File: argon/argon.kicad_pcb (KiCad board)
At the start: 2 copper layers, 60 x 60 mm, 77 parts, among them J1 USB, J2 V3V3-GND, J3 V3V3-GND, J4 V3V3-GND, J5 V3V3-GND, J6 V3V3-GND, J7 V3V3-GND, U1 LMC555xM, U2 AMS1117-3.3, U3 93LCxxA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

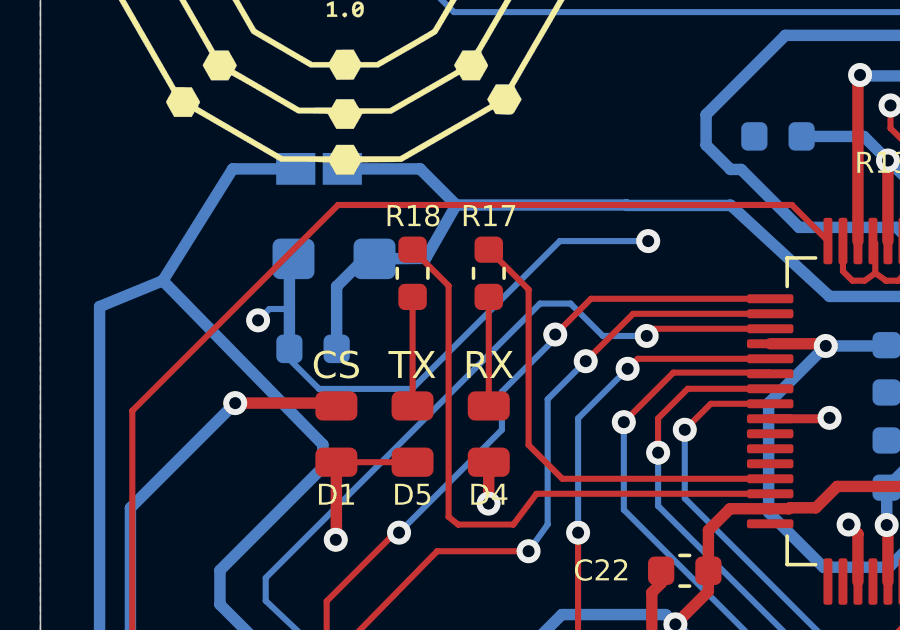
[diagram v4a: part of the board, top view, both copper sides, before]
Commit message: Small paths adjustments
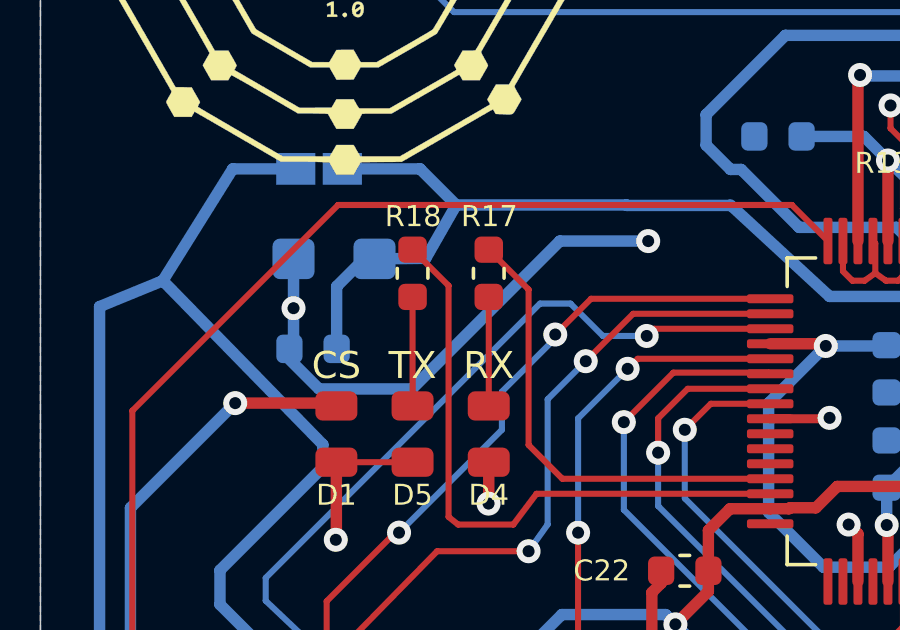
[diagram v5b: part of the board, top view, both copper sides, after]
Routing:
- net GND: track 122.4 -> 121.4 mm
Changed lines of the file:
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@@
     (thickness 1.6)
     (drawings 54)
-    (tracks 713)
+    (tracks 712)
     (zones 0)
     (modules 77)
@@
   (layers
     (0 F.Cu signal)
-    (31 B.Cu signal hide)
+    (31 B.Cu signal)
     (32 B.Adhes user hide)
     (33 F.Adhes user hide)
     (34 B.Paste user hide)
     (35 F.Paste user hide)
-    (36 B.SilkS user hide)
+    (36 B.SilkS user)
     (37 F.SilkS user)
     (38 B.Mask user hide)
@@
   )
   (setup
-    (last_trace_width 0.2032)
+    (last_trace_width 0.381)
     (user_trace_width 0.2032)
     (user_trace_width 0.3)
@@
   (segment (start 140.6905 114.7319) (end 140.38 115.0424) (width 0.381) (layer F.Cu) (net 1))
   (segment (start 140.6745 114.3) (end 140.6905 114.316) (width 0.381) (layer F.Cu) (net 1))
-  (segment (start 128.2985 104.0575) (end 128.436 103.92) (width 0.381) (layer B.Cu) (net 1))
   (segment (start 128.2985 106.92) (end 128.2985 107.2673) (width 0.2032) (layer B.Cu) (net 1))
-  (segment (start 128.2985 107.2673) (end 129.286 108.2548) (width 0.2032) (layer B.Cu) (net 1))
-  (segment (start 129.286 108.2548) (end 132.3848 108.2548) (width 0.2032) (layer B.Cu) (net 1))
-  (via (at 140.2588 103.3272) (size 0.8) (drill 0.4) (layers F.Cu B.Cu) (net 1))
-  (segment (start 132.3848 108.2548) (end 137.3124 103.3272) (width 0.2032) (layer B.Cu) (net 1))
-  (segment (start 137.3124 103.3272) (end 140.2588 103.3272) (width 0.2032) (layer B.Cu) (net 1))
-  (segment (start 128.2985 105.5909) (end 128.2985 104.0575) (width 0.381) (layer B.Cu) (net 1))
-  (segment (start 128.2985 106.92) (end 128.2985 105.5909) (width 0.381) (layer B.Cu) (net 1))
   (segment (start 160.655 97.393) (end 160.655 96.901) (width 0.2032) (layer F.Cu) (net 1))
   (segment (start 162.5 123.927) (end 162.5 125.028) (width 0.381) (layer B.Cu) (net 1))
@@
   (segment (start 149.7965 99.5045) (end 149.098 98.806) (width 0.2032) (layer B.Cu) (net 1))
   (segment (start 149.098 98.806) (end 148.336 98.806) (width 0.2032) (layer B.Cu) (net 1))
-  (segment (start 128.2985 105.5909) (end 127.6319 105.5909) (width 0.2032) (layer B.Cu) (net 1))
-  (segment (start 127.6319 105.5909) (end 127.254 105.9688) (width 0.2032) (layer B.Cu) (net 1))
-  (via (at 127.254 105.9688) (size 0.8) (drill 0.4) (layers F.Cu B.Cu) (net 1))
   (via (at 129.8448 113.284) (size 0.8) (drill 0.4) (layers F.Cu B.Cu) (net 1))
   (via (at 135.636 125.8316) (size 0.8) (drill 0.4) (layers F.Cu B.Cu) (net 1))
@@
   (segment (start 148.75 102.25) (end 148.75 102.216) (width 0.2032) (layer F.Cu) (net 1))
   (segment (start 148.75 103.325) (end 148.75 102.25) (width 0.2032) (layer F.Cu) (net 1))
+  (segment (start 128.2985 107.2673) (end 129.286 108.2548) (width 0.381) (layer B.Cu) (net 1))
+  (segment (start 129.286 108.2548) (end 132.3848 108.2548) (width 0.381) (layer B.Cu) (net 1))
+  (segment (start 132.3848 108.2548) (end 137.3124 103.3272) (width 0.381) (layer B.Cu) (net 1))
+  (segment (start 137.3124 103.3272) (end 140.2588 103.3272) (width 0.381) (layer B.Cu) (net 1))
+  (via (at 140.2588 103.3272) (size 0.8) (drill 0.4) (layers F.Cu B.Cu) (net 1))
+  (segment (start 128.2985 104.0575) (end 128.436 103.92) (width 0.381) (layer B.Cu) (net 1))
+  (segment (start 128.436 106.7825) (end 128.2985 106.92) (width 0.381) (layer B.Cu) (net 1))
+  (segment (start 128.436 103.92) (end 128.436 105.564) (width 0.381) (layer B.Cu) (net 1))
+  (segment (start 128.436 105.564) (end 128.436 106.7825) (width 0.381) (layer B.Cu) (net 1))
+  (via (at 128.436 105.564) (size 0.8) (drill 0.4) (layers F.Cu B.Cu) (net 1))
   (segment (start 136.503 121.9135) (end 137.687 120.7295) (width 0.381) (layer B.Cu) (net 2))
   (segment (start 134.9595 121.9135) (end 136.503 121.9135) (width 0.381) (layer B.Cu) (net 2))

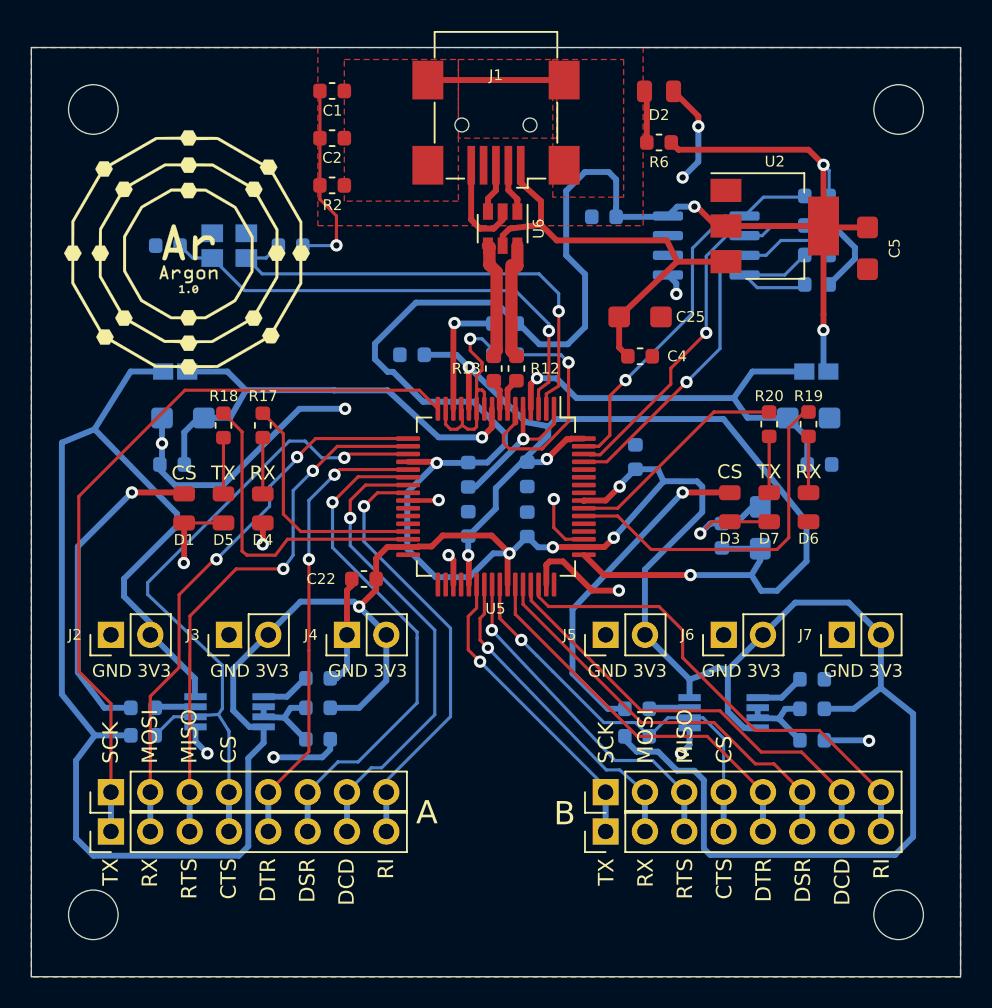
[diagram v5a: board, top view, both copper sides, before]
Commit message: Rounded corners
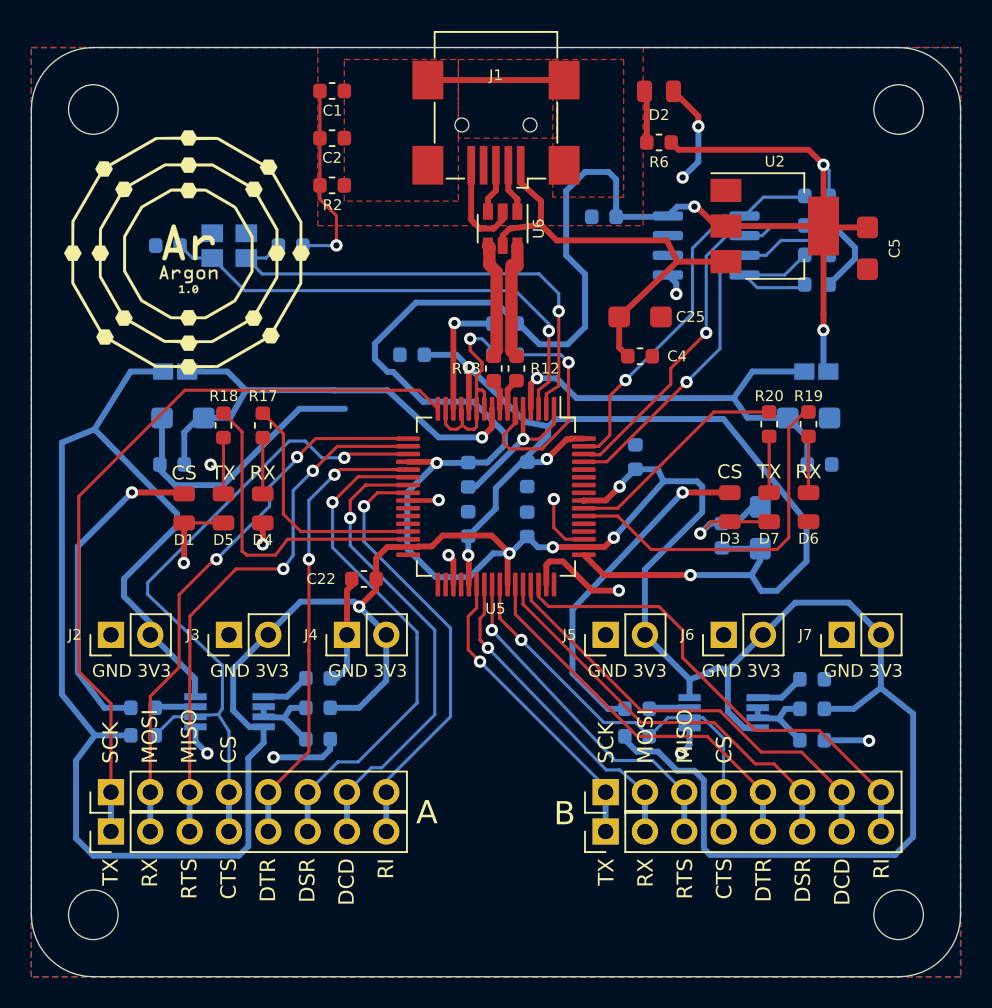
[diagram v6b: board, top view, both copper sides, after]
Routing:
- net GND: vias 19 -> 18
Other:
- outline, holes or cut-outs redrawn
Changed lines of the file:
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@@
   (general
     (thickness 1.6)
-    (drawings 54)
-    (tracks 712)
+    (drawings 58)
+    (tracks 710)
     (zones 0)
     (modules 77)
@@
   (page A4)
   (layers
-    (0 F.Cu signal)
+    (0 F.Cu signal hide)
     (31 B.Cu signal)
     (32 B.Adhes user hide)
@@
       (outputformat 1)
       (mirror false)
-      (drillshape 1)
+      (drillshape 0)
       (scaleselection 1)
-      (outputdirectory ""))
+      (outputdirectory "../gerber/"))
   )
   (net 0 "")
@@
     )
   )
+  (gr_arc (start 176 136) (end 176 140) (angle -90) (layer Edge.Cuts) (width 0.05))
+  (gr_arc (start 124 136) (end 120 136) (angle -90) (layer Edge.Cuts) (width 0.05))
+  (gr_arc (start 124 84) (end 124 80) (angle -90) (layer Edge.Cuts) (width 0.05))
+  (gr_arc (start 176 84) (end 180 84) (angle -90) (layer Edge.Cuts) (width 0.05))
   (gr_text MOSI (at 159.654 126.25 90) (layer F.SilkS)
     (effects (font (size 1 1) (thickness 0.2)) (justify left))
@@
     (effects (font (size 0.9 0.9) (thickness 0.2)))
   )
-  (gr_line (start 120 140) (end 120 80) (layer Edge.Cuts) (width 0.05))
-  (gr_line (start 180 140) (end 120 140) (layer Edge.Cuts) (width 0.05))
-  (gr_line (start 180 80) (end 180 140) (layer Edge.Cuts) (width 0.05))
-  (gr_line (start 120 80) (end 180 80) (layer Edge.Cuts) (width 0.05))
+  (gr_line (start 120 136) (end 120 84) (layer Edge.Cuts) (width 0.05))
+  (gr_line (start 176 140) (end 124 140) (layer Edge.Cuts) (width 0.05))
+  (gr_line (start 180 84) (end 180 136) (layer Edge.Cuts) (width 0.05))
+  (gr_line (start 124 80) (end 176 80) (layer Edge.Cuts) (width 0.05))
   (segment (start 150.4315 90.594) (end 150.4315 91.1225) (width 0.381) (layer F.Cu) (net 1))
   (segment (start 150.4315 91.1225) (end 149.86 91.694) (width 0.381) (layer F.Cu) (net 1))
@@
   (segment (start 132.3848 108.2548) (end 137.3124 103.3272) (width 0.381) (layer B.Cu) (net 1))
   (segment (start 137.3124 103.3272) (end 140.2588 103.3272) (width 0.381) (layer B.Cu) (net 1))
-  (via (at 140.2588 103.3272) (size 0.8) (drill 0.4) (layers F.Cu B.Cu) (net 1))
   (segment (start 128.2985 104.0575) (end 128.436 103.92) (width 0.381) (layer B.Cu) (net 1))
   (segment (start 128.436 106.7825) (end 128.2985 106.92) (width 0.381) (layer B.Cu) (net 1))
-  (segment (start 128.436 103.92) (end 128.436 105.564) (width 0.381) (layer B.Cu) (net 1))
-  (segment (start 128.436 105.564) (end 128.436 106.7825) (width 0.381) (layer B.Cu) (net 1))
-  (via (at 128.436 105.564) (size 0.8) (drill 0.4) (layers F.Cu B.Cu) (net 1))
+  (segment (start 128.436 103.92) (end 128.436 106.7825) (width 0.381) (layer B.Cu) (net 1))
+  (via (at 131.572 106.934) (size 0.8) (drill 0.4) (layers F.Cu B.Cu) (net 1))
   (segment (start 136.503 121.9135) (end 137.687 120.7295) (width 0.381) (layer B.Cu) (net 2))
   (segment (start 134.9595 121.9135) (end 136.503 121.9135) (width 0.381) (layer B.Cu) (net 2))

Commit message: Move everything to make more place for labels
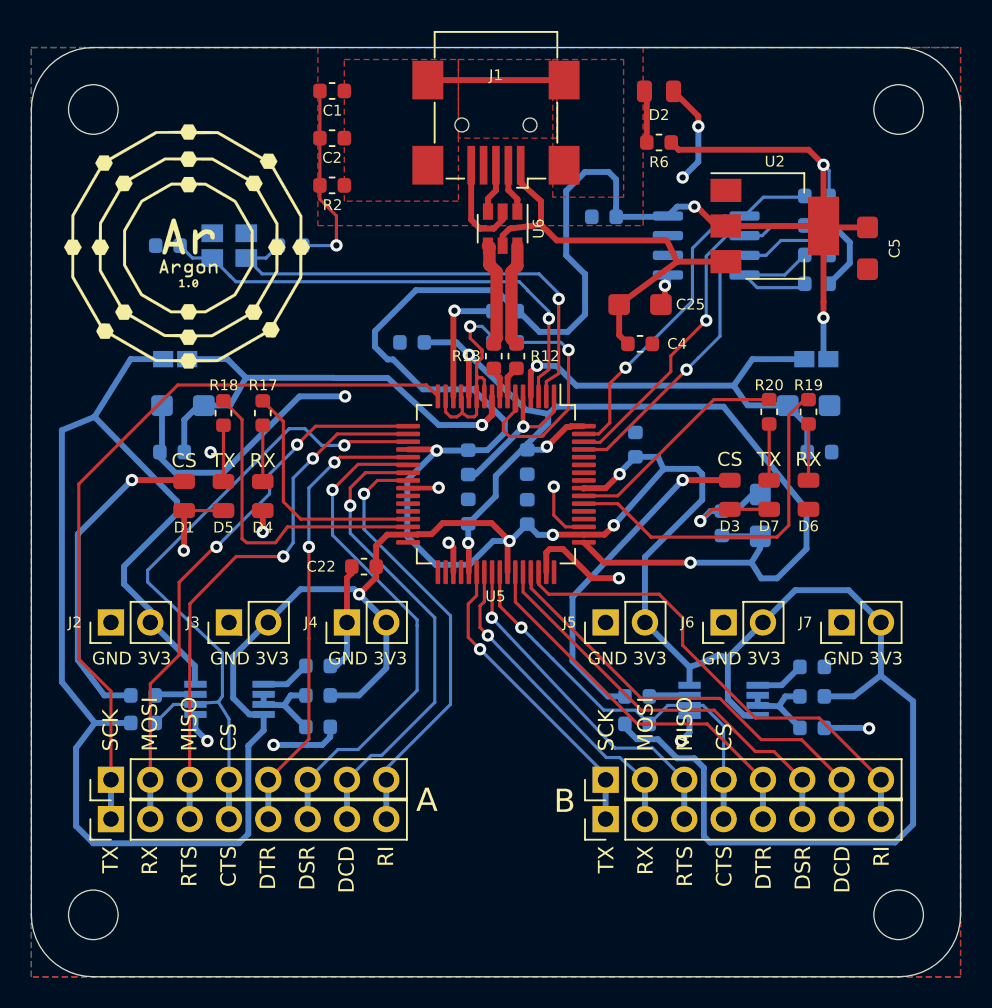
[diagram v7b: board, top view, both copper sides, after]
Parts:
- moved C20 0.80 mm to (148.2, 110.0)
- moved C4 0.80 mm to (159.3, 99.1)
- moved C8 0.80 mm to (164.6, 110.7)
- moved C9 0.80 mm to (170.4, 120.0)
- moved D1 0.80 mm to (129.9, 109.0)
- moved D3 0.80 mm to (165.1, 108.9)
- moved D4 0.80 mm to (134.9, 109.0)
- moved D5 0.80 mm to (132.4, 109.0)
- moved D6 0.80 mm to (170.2, 108.9)
- moved D7 0.80 mm to (167.6, 108.9)
- moved S1 0.80 mm to (125.1, 129.8)
- moved S2 0.80 mm to (157.1, 129.8)
- moved S3 0.80 mm to (125.1, 127.3)
- moved S4 0.80 mm to (157.1, 127.3)
- moved C12 0.80 mm to (129.8, 103.1)
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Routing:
- net V3V3: track 339.1 -> 337.2 mm
- net Net-(R12-Pad2): track 7.82 -> 6.59 mm
- net Net-(C10-Pad1): track 31.4 -> 30.3 mm
- net Net-(R7-Pad1): track 24.3 -> 23.5 mm
- net Net-(R8-Pad1): track 25.3 -> 24.5 mm
- net Net-(R9-Pad1): track 24.9 -> 24.1 mm
- net Net-(R13-Pad2): track 7.54 -> 6.74 mm
- net GND: track 121.4 -> 122.0 mm, vias 18 -> 19
- net VBUS: track 29.4 -> 28.9 mm
